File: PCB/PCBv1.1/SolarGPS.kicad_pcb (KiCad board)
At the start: 2 copper layers, 73 x 27 mm, 54 parts, among them J1 Conn_01x10_Female, J2 Solar1+, J3 GND, J4 Conn_02x05_Odd_Even, J5 Solar2+, J6 GND, J7 Screw_Terminal_01x01, U2 MAX-M10Q, U4 STM32WB5MMGH6TR, U5 BQ25505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

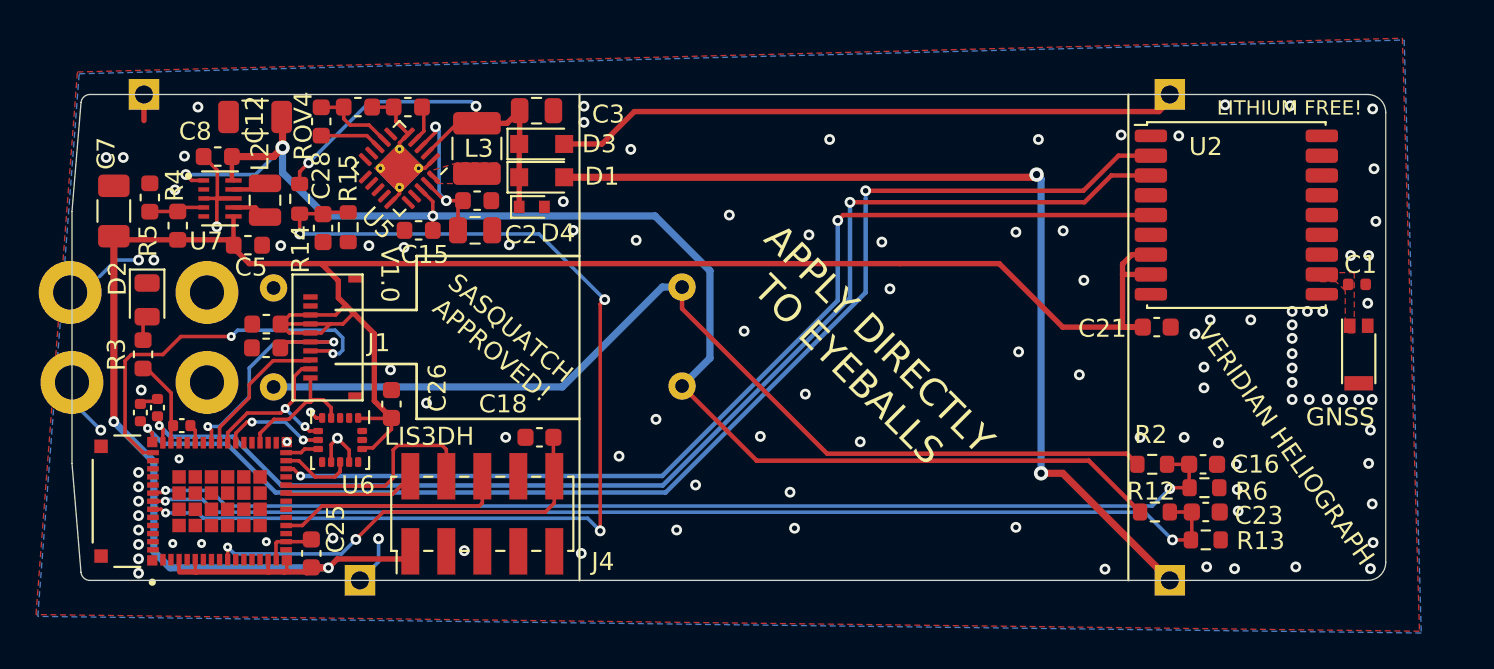
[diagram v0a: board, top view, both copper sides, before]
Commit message: Change VCC to 2.87 Remove LCD connector
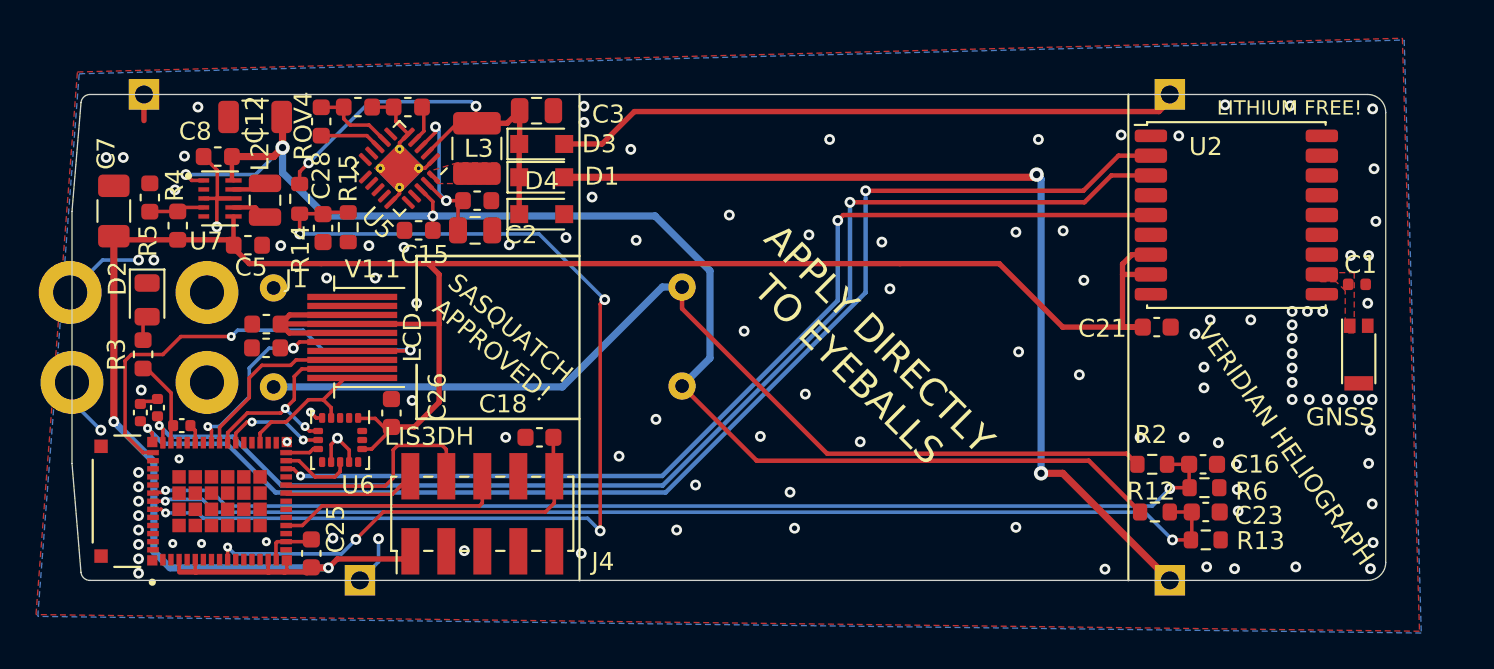
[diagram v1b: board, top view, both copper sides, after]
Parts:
- D4: footprint Diode_SMD:D_SOD-523 -> Diode_SMD:D_SOD-323_HandSoldering
- J1: footprint Margo_Lib:AYF531035 -> Veridian Designed:0.5pFlexToBoard
- moved J1 1.32 mm to (63.6, 63.5)
- moved D4 0.68 mm to (75.1, 56.6)
- moved C26 0.50 mm to (66.8, 67.7)
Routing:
- net VDD: track 139.9 -> 146.1 mm
- net EXTCOMIN: track 21.7 -> 26.4 mm
- net DISP_CS: track 7.88 -> 10.4 mm
- net SPI_MOSI: track 9.72 -> 12.0 mm
- net GND: track 31.0 -> 33.2 mm, vias 108 -> 110
- net DISP_EN: track 14.0 -> 12.6 mm
- net SPI_CLK: track 7.35 -> 8.11 mm
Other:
- board text added: "V1.1"
- board text removed: "V1.0"

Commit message: Cost savings!
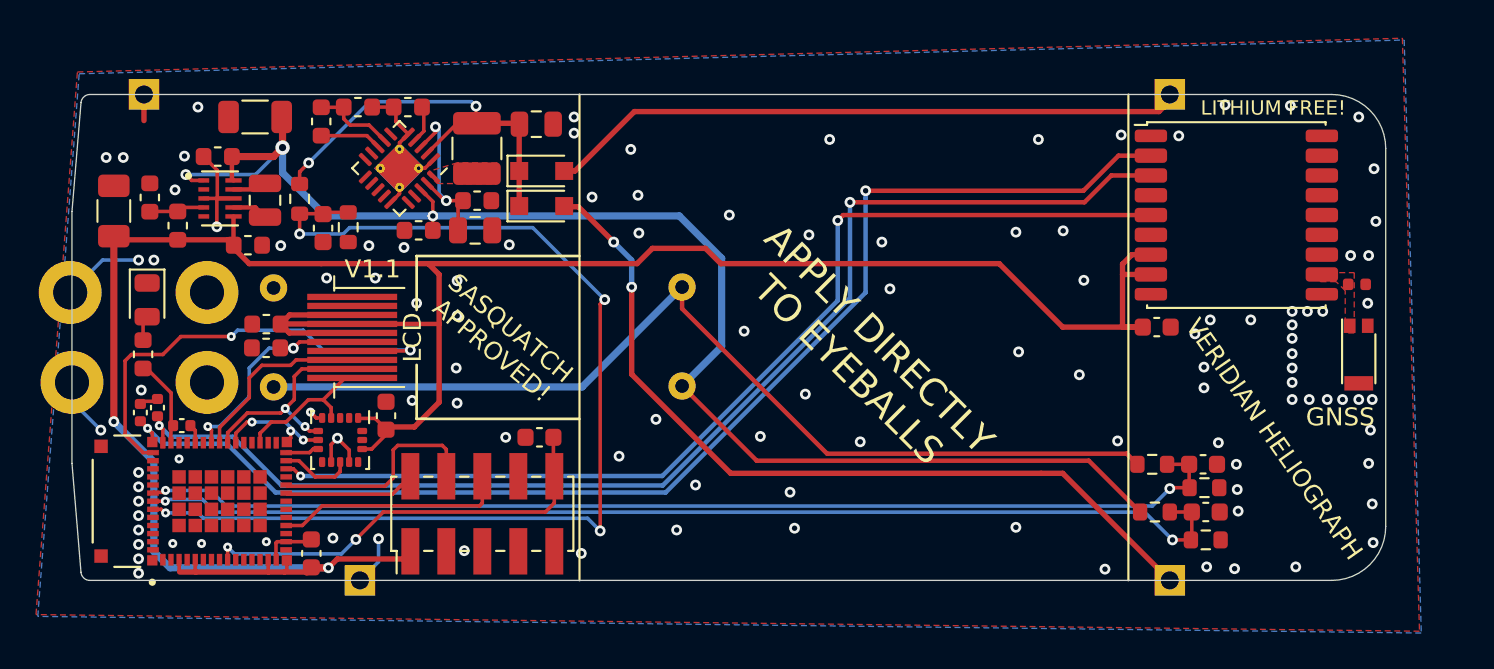
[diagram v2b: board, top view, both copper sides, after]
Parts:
- removed D4: 5.1V, Diode_SMD:D_SOD-323_HandSoldering
- moved D1 1.60 mm to (75.1, 56.2)
- moved D3 1.50 mm to (75.1, 54.2)
- moved C3 0.75 mm to (74.8, 51.6)
- moved C26 0.34 mm to (66.5, 67.8)
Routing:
- net Net-(D1-Pad2): track 52.1 -> 45.5 mm
- net VBAT: track 78.6 -> 79.9 mm
- net SOLAR+: track 24.6 -> 23.8 mm
- net VDD: track 146.1 -> 146.8 mm
- net GND: track 33.2 -> 33.9 mm, vias 110 -> 112
- net Net-(D3-Pad2): track 34.5 -> 35.1 mm
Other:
- outline, holes or cut-outs redrawn

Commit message: Play with USB idea. Update to KiCad 5
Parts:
- removed C18: 10nF, Capacitor_SMD:C_0603_1608Metric
- added C27: 10nF, Capacitor_SMD:C_0603_1608Metric, F.Cu at (75.8, 69.9)
- added R7: 91k, Resistor_SMD:R_0603_1608Metric, F.Cu at (64.9, 74.3)
- J4: footprint Connector_PinHeader_2.00mm:PinHeader_2x05_P2.00mm_Vertical_SMD -> Connector:Tag-Connect_TC2050-IDC-NL_2x05_P1.27mm_Vertical
- R4: value 412k -> 432k
- moved AE1 2.35 mm to (122.8, 64.5)
- moved C1 1.03 mm to (120.3, 59.5), turned to -90 degrees
- moved J4 0.17 mm to (71.8, 73.1), turned to 180 degrees
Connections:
- U2 pad 6: Net-(U2-Pad6) -> VDD
- U4 pad 13: Net-(U4-Pad13) -> BOOT0
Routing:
- net RESET: track 23.8 -> 33.0 mm
- net BOOT0: track 0.00 -> 7.97 mm, vias 0 -> 2
- net VDD: track 146.8 -> 153.5 mm
- net /GPS_RF: track 0.00 -> 5.81 mm
- net /SWDIO: track 7.34 -> 12.8 mm
- net /SWO: track 12.9 -> 9.40 mm
- net VBAT_SENSE: track 61.5 -> 63.4 mm
- net VBATMID_SENSE: track 60.9 -> 62.8 mm
- net GND: track 33.9 -> 32.3 mm
- net SOLAR_SENSE1: track 60.8 -> 62.1 mm
- net /SWDCLK: track 12.4 -> 11.5 mm
- removed copper zone on F.Cu, net /GPS_RF
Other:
- board size 73 x 27 mm -> 75 x 27 mm
- net class Default removed
- net class VDD removed

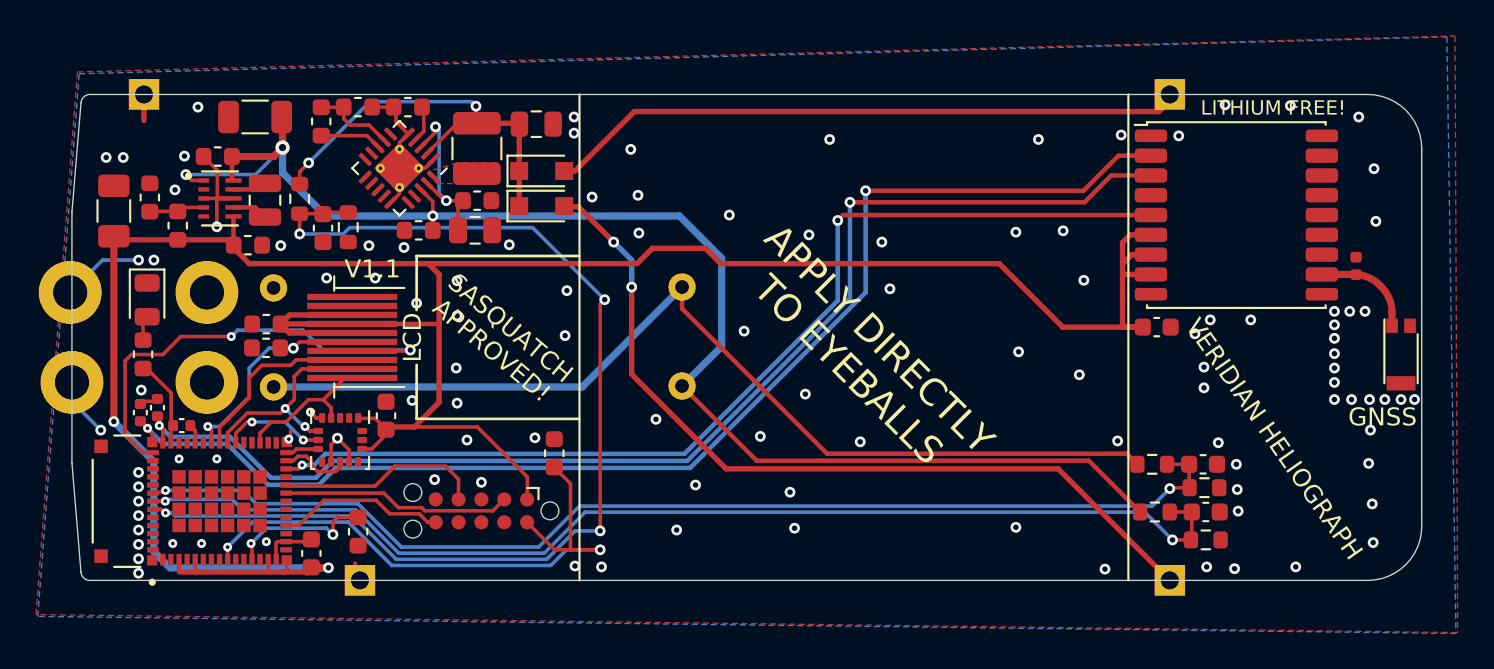
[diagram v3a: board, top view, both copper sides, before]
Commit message: Add more App, DropBLE
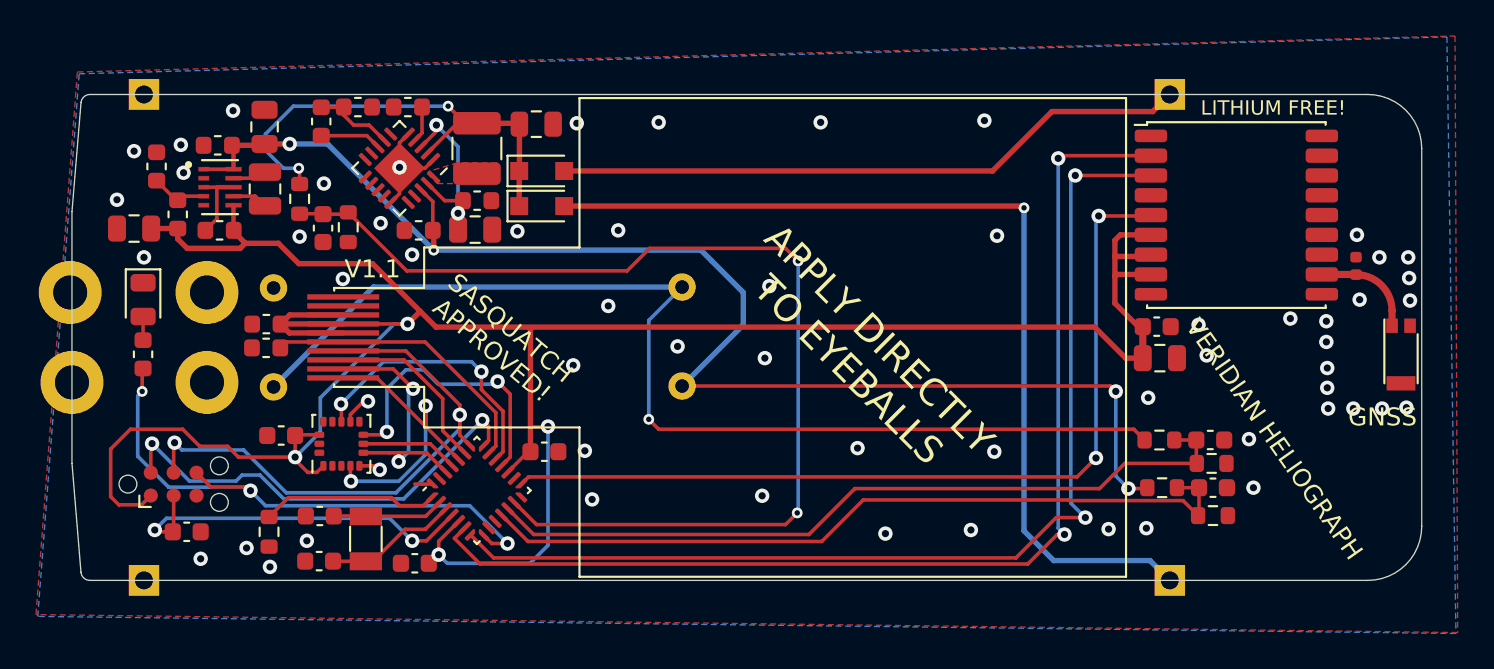
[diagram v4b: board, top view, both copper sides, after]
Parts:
- removed C27: 10nF, Capacitor_SMD:C_0603_1608Metric
- removed R7: 91k, Resistor_SMD:R_0603_1608Metric
- removed U4: STM32WB5MMGH6TR, Veridian-Library-KiCad:XCVR_STM32WB5MMGH6TR
- added C18: 10nF, Capacitor_SMD:C_0603_1608Metric, F.Cu at (55.4, 74.3)
- added C4: 11pF, Capacitor_SMD:C_0603_1608Metric, F.Cu at (62.8, 73.4)
- added R1: 91k, Resistor_SMD:R_0603_1608Metric, F.Cu at (60.0, 74.3)
- added U1: STM32L011G3Ux, Package_DFN_QFN:QFN-28_4x4mm_P0.5mm, F.Cu at (71.5, 72.0)
- added Y1: 32.768, Crystal:Crystal_SMD_3215-2Pin_3.2x1.5mm, F.Cu at (65.3, 74.7)
- C10: value 3.3pF -> 11pF; footprint Capacitor_SMD:C_0402_1005Metric -> Capacitor_SMD:C_0603_1608Metric
- C11: value 3.3pF -> 1uF; footprint Capacitor_SMD:C_0402_1005Metric -> Capacitor_SMD:C_0603_1608Metric
- C12, C7: value 100uF -> 47uF; footprint Capacitor_SMD:C_1206_3216Metric -> Capacitor_SMD:C_0805_2012Metric
- C13: value 3.3pF -> 4.7uF; footprint Capacitor_SMD:C_0402_1005Metric -> Capacitor_SMD:C_0805_2012Metric
- J1: footprint Veridian Designed:0.5pFlexToBoard -> Margo_Lib:LS013B7DH03
- J4: value Conn_02x05_Odd_Even -> Conn_02x03_Odd_Even; footprint Connector:Tag-Connect_TC2050-IDC-NL_2x05_P1.27mm_Vertical -> Connector:Tag-Connect_TC2030-IDC-NL_2x03_P1.27mm_Vertical
- R4: value 432k -> 412k
- U5: footprint Package_DFN_QFN:QFN-20-1EP_3.5x3.5mm_P0.5mm_EP2x2mm_ThermalVias -> Package_DFN_QFN:QFN-20-1EP_3.5x3.5mm_P0.5mm_EP2x2mm
- moved C13 55.8 mm to (109.5, 64.7), turned to 0 degrees
- moved C11 22.6 mm to (75.2, 69.8), turned to 0 degrees
- moved J4 17.2 mm to (54.6, 71.7), turned to 0 degrees
- moved J6 12.0 mm to (53.0, 77.0)
- moved C10 10.7 mm to (62.7, 75.9)
- moved C26 5.93 mm to (60.6, 69.0), turned to 0 degrees
- moved C25 5.78 mm to (68.0, 76.0), turned to 180 degrees
- moved C5 1.78 mm to (57.2, 57.5), turned to 0 degrees
- moved R5 1.77 mm to (53.7, 54.0)
- moved C7 1.49 mm to (52.5, 57.5), turned to 0 degrees
- moved C23 1.41 mm to (112.4, 71.8)
- moved R12 1.41 mm to (109.6, 71.8)
- moved C16 1.41 mm to (112.2, 69.2)
- moved R13 1.41 mm to (112.4, 73.4)
- moved R6 1.41 mm to (112.3, 70.5)
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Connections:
- C10 pad 1: GND -> Net-(C10-Pad1)
- C10 pad 2: LED -> GND
- C11 pad 1: GND -> VDD
- C11 pad 2: GPS_UART_MISO -> GND
- C13 pad 1: GND -> VDD
- C13 pad 2: GPS_UART_MOSI -> GND
- J4 pad 3: GND -> RESET
- J4 pad 4: /SWDCLK -> EXTCOMIN
- J4 pad 6: /SWO -> LED
- U2 pad 13: Net-(U2-Pad13) -> unconnected-(U2-Pad13)
- U2 pad 14: Net-(U2-Pad14) -> unconnected-(U2-Pad14)
- U2 pad 15: Net-(U2-Pad15) -> unconnected-(U2-Pad15)
- U2 pad 16: Net-(U2-Pad16) -> unconnected-(U2-Pad16)
- U2 pad 17: Net-(U2-Pad17) -> unconnected-(U2-Pad17)
- U2 pad 18: Net-(U2-Pad18) -> unconnected-(U2-Pad18)
- U2 pad 4: Net-(U2-Pad4) -> unconnected-(U2-Pad4)
- U2 pad 9: Net-(U2-Pad9) -> unconnected-(U2-Pad9)
- U5 pad 10: Net-(U5-Pad10) -> unconnected-(U5-Pad10)
- U5 pad 11: Net-(U5-Pad11) -> unconnected-(U5-Pad11)
- U5 pad 12: Net-(U5-Pad12) -> unconnected-(U5-Pad12)
- U5 pad 13: Net-(U5-Pad13) -> unconnected-(U5-Pad13)
- U5 pad 14: Net-(U5-Pad14) -> unconnected-(U5-Pad14)
- U5 pad 16: Net-(U5-Pad16) -> unconnected-(U5-Pad16)
- U5 pad 17: Net-(U5-Pad17) -> unconnected-(U5-Pad17)
- U5 pad 6: Net-(U5-Pad6) -> unconnected-(U5-Pad6)
- U5 pad 9: Net-(U5-Pad9) -> unconnected-(U5-Pad9)
- U6 pad 13: Net-(U6-Pad13) -> unconnected-(U6-Pad13)
- U6 pad 15: Net-(U6-Pad15) -> unconnected-(U6-Pad15)
- U6 pad 16: Net-(U6-Pad16) -> unconnected-(U6-Pad16)
- U6 pad 2: Net-(U6-Pad2) -> unconnected-(U6-Pad2)
- U6 pad 3: Net-(U6-Pad3) -> unconnected-(U6-Pad3)
- U6 pad 9: Net-(U6-Pad9) -> unconnected-(U6-Pad9)
- U7 pad 5: Net-(U7-Pad5) -> unconnected-(U7-Pad5)
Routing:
- net LED: track 5.09 -> 32.5 mm, vias 0 -> 3
- net GND: track 32.3 -> 11.1 mm, vias 112 -> 59
- net VBAT_SENSE: track 63.4 -> 43.4 mm, vias 2 -> 0
- net VBATMID_SENSE: track 62.8 -> 43.0 mm, vias 2 -> 0
- net LIS_CS: track 1.86 -> 15.9 mm, vias 0 -> 2
- net /SWDIO: track 12.8 -> 25.0 mm, vias 0 -> 2
- net RESET: track 33.0 -> 21.0 mm
- net LIS_INT: track 3.96 -> 15.5 mm, vias 0 -> 2
- net /SWDCLK: track 11.5 -> 0.00 mm
- net SPI_CLK: track 8.11 -> 17.8 mm, vias 0 -> 2
- net /SWO: track 9.40 -> 0.00 mm
- net GPS_UART_MOSI: track 68.2 -> 59.3 mm
- net GPS_EXINT: track 56.5 -> 49.0 mm
- net Net-(C10-Pad1): track 0.00 -> 7.48 mm
- net Net-(D1-Pad2): track 45.5 -> 52.5 mm, vias 2 -> 1
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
